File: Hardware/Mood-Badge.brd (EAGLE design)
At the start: 100 x 80 mm, 33 parts, among them J1 AVR_SPI_PROG_3X2NS, J2 FTDI_DEVICE, SW2 SWITCH.JS202011JXQNUPWARDS, SW3 SWITCH.JS202011JXQNUPWARDS, U1 ATMEGA328P_TQFP

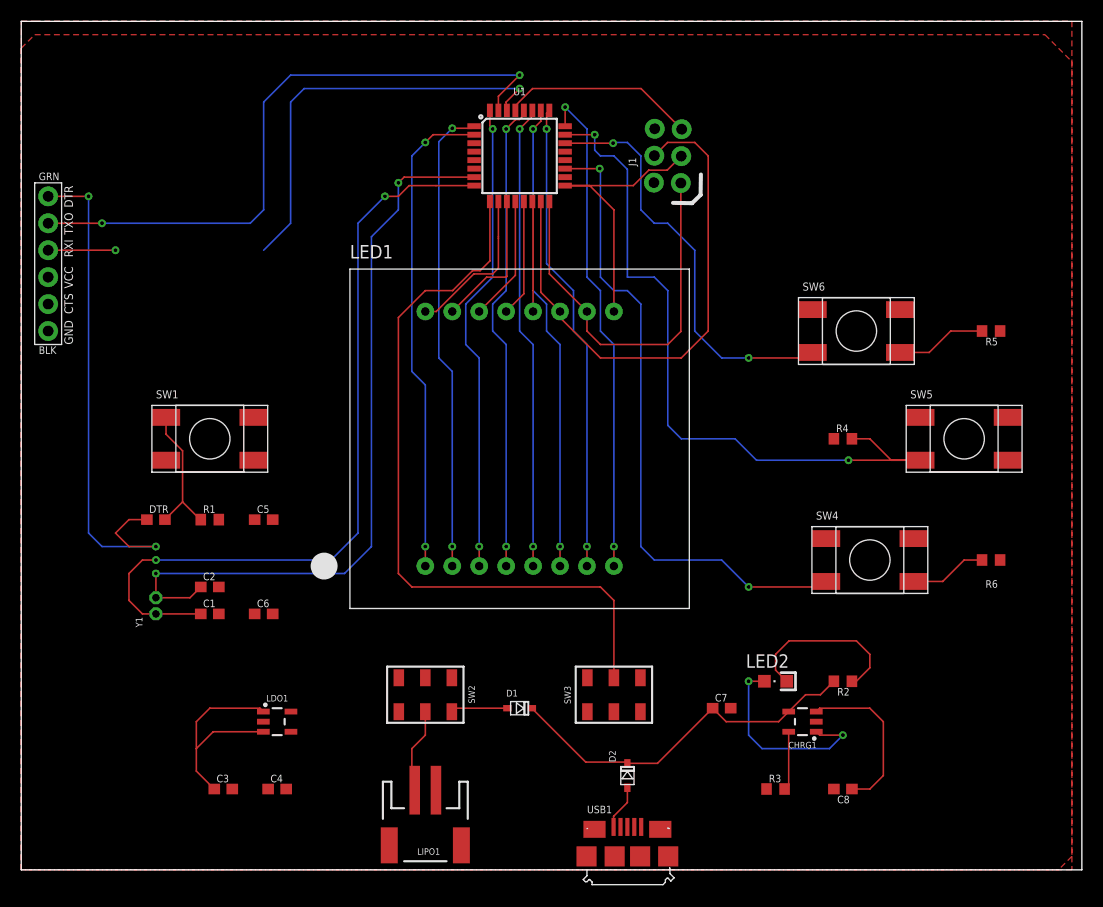
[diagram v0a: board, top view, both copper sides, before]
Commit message: drc errors fixed
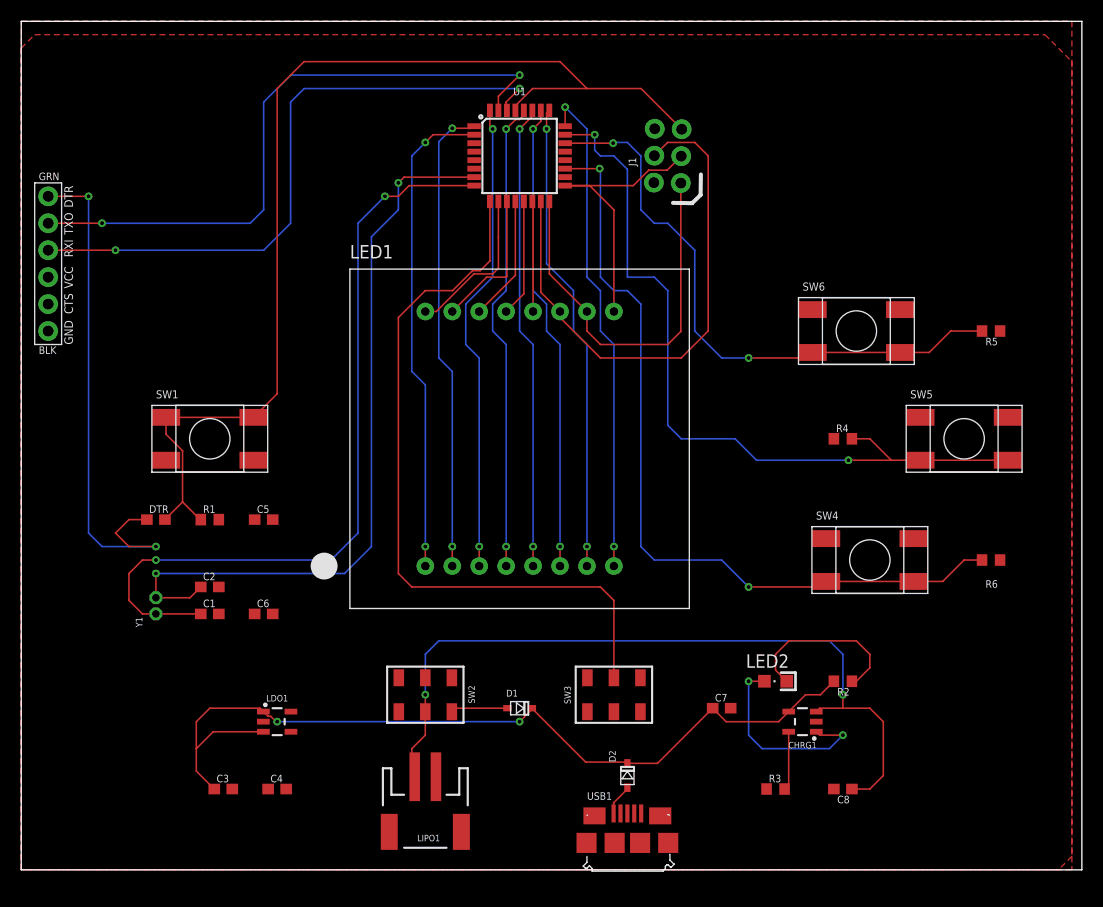
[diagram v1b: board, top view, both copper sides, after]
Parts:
- moved LIPO1 1.27 mm to (38.1, 5.08)
- moved USB1 1.27 mm to (57.1, 3.81)
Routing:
- net RESET: track 31.8 -> 103.2 mm
- net VLIPO: track 23.9 -> 73.2 mm, vias 0 -> 2
- net VIN: track 56.2 -> 82.2 mm, vias 0 -> 2
- net RXD: track 46.1 -> 60.1 mm
- net RIGHT: track 48.1 -> 56.2 mm
- net ACTION: track 67.9 -> 76.0 mm
- net LEFT: track 68.2 -> 73.3 mm
- net V_USB: track 4.23 -> 2.96 mm
